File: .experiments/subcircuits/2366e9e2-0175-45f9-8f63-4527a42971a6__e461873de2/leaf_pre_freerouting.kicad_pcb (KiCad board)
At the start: 2 copper layers, 49.9 x 20.9 mm, 7 parts, among them J2 Output, J3 Debug, U5 AP2112K-3.3

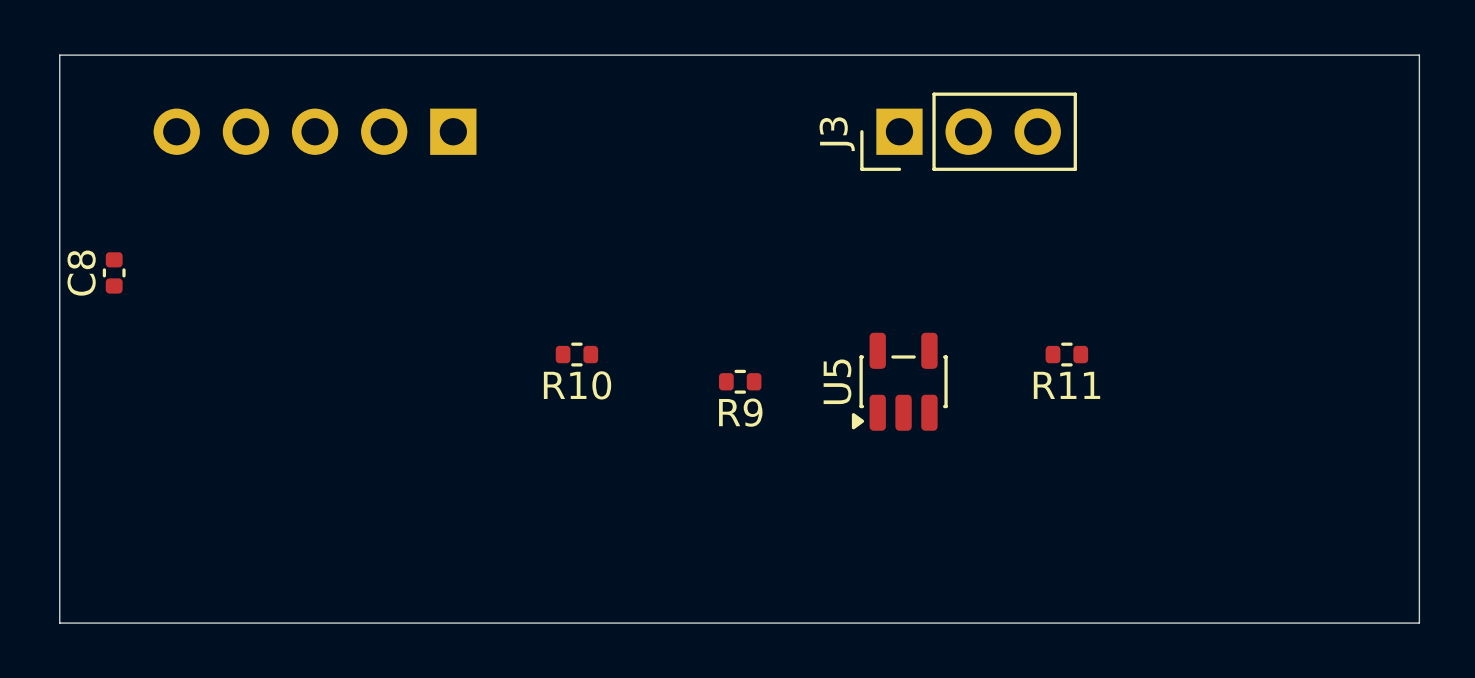
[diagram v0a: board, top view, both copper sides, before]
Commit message: feat: parent board stamping with preserved child copper
- Add --pcb, --stamp, --route, --jar flags to compose_subcircuits.py
- Implement subprocess-based parent board stamping (no pcbnew in main process)
- Add _stamp_parent_board() that copies base PCB, moves footprints to
  composed positions, clears existing tracks/zones, recreates child copper
  traces and vias with proper net name resolution
- Add _route_parent_board() for FreeRouting with preserve_existing_copper
- Add _persist_parent_artifact() for parent solved_layout.json persistence
- Store ParentComposition on ParentCompositionState for downstream access
- Update leaf artifacts from fresh pipeline run (6/6 leaves routed)
- Parent stamp verified: 37 components, 286 child traces, 10 vias preserved
  on real .kicad_pcb board with correct positions and net assignments
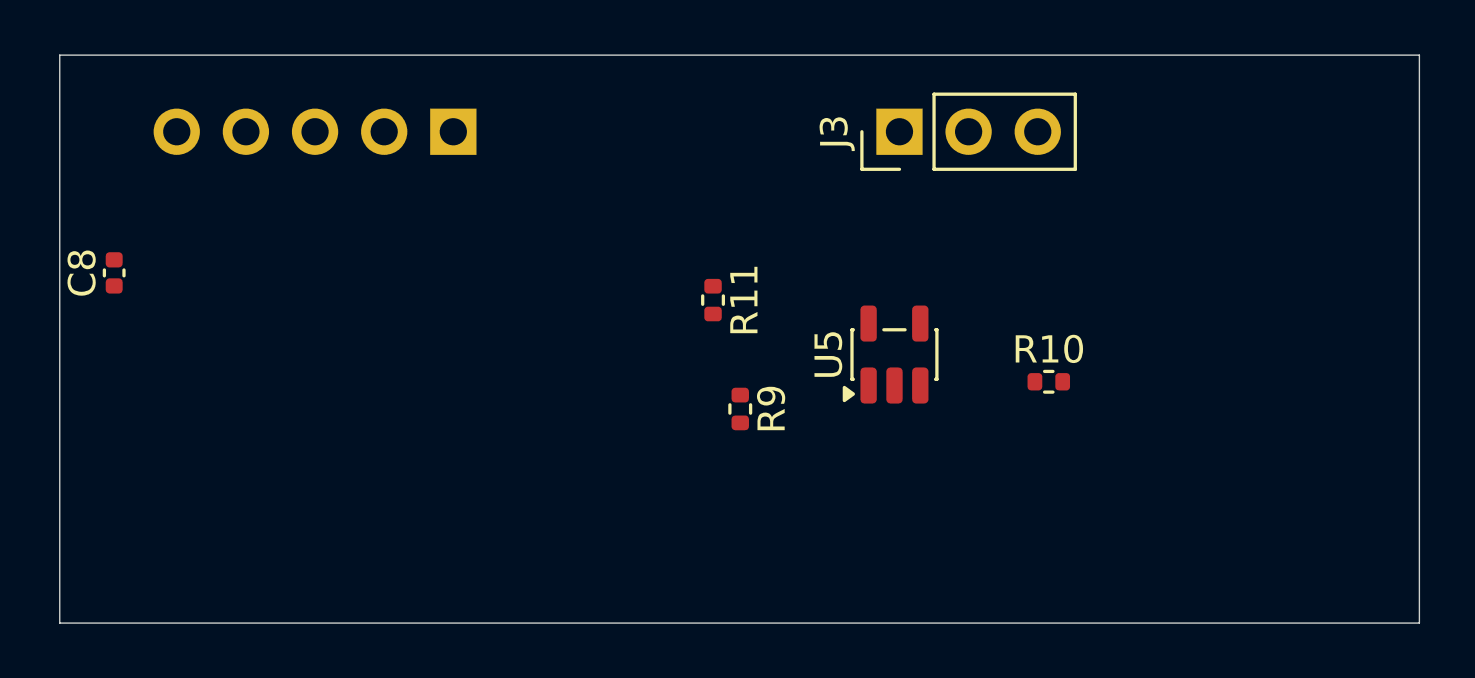
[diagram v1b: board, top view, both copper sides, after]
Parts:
- moved R10 17.4 mm to (36.3, 12.0), turned to 0 degrees
- moved R11 13.2 mm to (24.0, 9.00), turned to -90 degrees
- moved U5 1.05 mm to (30.7, 11.0)
- moved R9 1.00 mm to (25.0, 13.0), turned to -90 degrees
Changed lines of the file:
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@@
 	(footprint "Resistor_SMD:R_0402_1005Metric"
 		(layer "F.Cu")
-		(at 37 11 180)
+		(at 24 9 -90)
 		(descr "Resistor SMD 0402 (1005 Metric), square (rectangular) end terminal, IPC-7351 nominal, (Body size source: IPC-SM-782 page 72, https://www.pcb-3d.com/wordpress/wp-content/uploads/ipc-sm-782a_amendment_1_and_2.pdf), generated with kicad-footprint-generator")
 		(tags "resistor")
 		(property "Reference" "R11"
-			(at 0 -1.17 180)
+			(at 0 -1.17 270)
 			(layer "F.SilkS")
 			(effects
@@
 		)
 		(property "Value" "100k"
-			(at 0 1.17 180)
+			(at 0 1.17 270)
 			(layer "F.Fab")
 			(effects
@@
 		)
 		(property "Datasheet" ""
-			(at 0 0 180)
+			(at 0 0 270)
 			(layer "F.Fab")
 			(hide yes)
@@
 		)
 		(property "Description" ""
-			(at 0 0 180)
+			(at 0 0 270)
 			(layer "F.Fab")
 			(hide yes)
@@
 		)
 		(fp_text user "${REFERENCE}"
-			(at 0 0 180)
+			(at 0 0 270)
 			(layer "F.Fab")
 			(effects
@@
 		)
 		(pad "1" smd roundrect
-			(at -0.51 0 180)
+			(at -0.51 0 270)
 			(size 0.54 0.64)
 			(layers "F.Cu" "F.Mask" "F.Paste")
@@
 		)
 		(pad "2" smd roundrect
-			(at 0.51 0 180)
+			(at 0.51 0 270)
 			(size 0.54 0.64)
 			(layers "F.Cu" "F.Mask" "F.Paste")
@@
 	(footprint "Resistor_SMD:R_0402_1005Metric"
 		(layer "F.Cu")
-		(at 25 12 180)
+		(at 25 13 -90)
 		(descr "Resistor SMD 0402 (1005 Metric), square (rectangular) end terminal, IPC-7351 nominal, (Body size source: IPC-SM-782 page 72, https://www.pcb-3d.com/wordpress/wp-content/uploads/ipc-sm-782a_amendment_1_and_2.pdf), generated with kicad-footprint-generator")
 		(tags "resistor")
 		(property "Reference" "R9"
-			(at 0 -1.17 180)
+			(at 0 -1.17 270)
 			(layer "F.SilkS")
 			(effects
@@
 		)
 		(property "Value" "75k"
-			(at 0 1.17 180)
+			(at 0 1.17 270)
 			(layer "F.Fab")
 			(effects
@@
 		)
 		(property "Datasheet" ""
-			(at 0 0 180)
+			(at 0 0 270)
 			(layer "F.Fab")
 			(hide yes)
@@
 		)
 		(property "Description" ""
-			(at 0 0 180)
+			(at 0 0 270)
 			(layer "F.Fab")
 			(hide yes)
@@
 		)
 		(fp_text user "${REFERENCE}"
-			(at 0 0 180)
+			(at 0 0 270)
 			(layer "F.Fab")
 			(effects
@@
 		)
 		(pad "1" smd roundrect
-			(at -0.51 0 180)
+			(at -0.51 0 270)
 			(size 0.54 0.64)
 			(layers "F.Cu" "F.Mask" "F.Paste")
@@
 		)
 		(pad "2" smd roundrect
-			(at 0.51 0 180)
+			(at 0.51 0 270)
 			(size 0.54 0.64)
 			(layers "F.Cu" "F.Mask" "F.Paste")
@@
 	(footprint "Resistor_SMD:R_0402_1005Metric"
 		(layer "F.Cu")
-		(at 19 11 180)
+		(at 36.335 12)
 		(descr "Resistor SMD 0402 (1005 Metric), square (rectangular) end terminal, IPC-7351 nominal, (Body size source: IPC-SM-782 page 72, https://www.pcb-3d.com/wordpress/wp-content/uploads/ipc-sm-782a_amendment_1_and_2.pdf), generated with kicad-footprint-generator")
 		(tags "resistor")
 		(property "Reference" "R10"
-			(at 0 -1.17 180)
+			(at 0 -1.17 0)
 			(layer "F.SilkS")
 			(effects
@@
 		)
 		(property "Value" "10k"
-			(at 0 1.17 180)
+			(at 0 1.17 0)
 			(layer "F.Fab")
 			(effects
@@
 		)
 		(property "Datasheet" ""
-			(at 0 0 180)
+			(at 0 0 0)
 			(layer "F.Fab")
 			(hide yes)
@@
 		)
 		(property "Description" ""
-			(at 0 0 180)
+			(at 0 0 0)
 			(layer "F.Fab")
 			(hide yes)
@@
 		)
 		(attr smd)
+		(fp_line
+			(start -0.153641 -0.38)
+			(end 0.153641 -0.38)
+			(stroke
+				(width 0.12)
+				(type solid)
+			)
+			(layer "F.SilkS")
+		)
 		(fp_line
 			(start -0.153641 0.38)
@@
 			(layer "F.SilkS")
 		)
-		(fp_line
-			(start -0.153641 -0.38)
-			(end 0.153641 -0.38)
-			(stroke
-				(width 0.12)
-				(type solid)
-			)
-			(layer "F.SilkS")
-		)
 		(fp_rect
 			(start -0.93 -0.47)
@@
 		)
 		(fp_text user "${REFERENCE}"
-			(at 0 0 180)
+			(at 0 0 0)
 			(layer "F.Fab")
 			(effects
@@
 		)
 		(pad "1" smd roundrect
-			(at -0.51 0 180)
+			(at -0.51 0)
 			(size 0.54 0.64)
 			(layers "F.Cu" "F.Mask" "F.Paste")
@@
 		)
 		(pad "2" smd roundrect
-			(at 0.51 0 180)
+			(at 0.51 0)
 			(size 0.54 0.64)
 			(layers "F.Cu" "F.Mask" "F.Paste")
@@
 	(footprint "Package_TO_SOT_SMD:SOT-23-5"
 		(layer "F.Cu")
-		(at 31 12 90)
+		(at 30.665 11 90)
 		(descr "SOT, 5 Pin (JEDEC MO-178 Var AA https://www.jedec.org/document_search?search_api_views_fulltext=MO-178), generated with kicad-footprint-generator ipc_gullwing_generator.py")
 		(tags "SOT TO_SOT_SMD")

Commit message: feat: unified hierarchical solver (solve_hierarchy.py)
Single-command entry point for the full subcircuit pipeline:
  python3 solve_hierarchy.py LLUPS.kicad_sch --pcb LLUPS.kicad_pcb --route

Phase 1: Solve leaf subcircuits (delegates to solve_subcircuits.py)
  - 6 leaves solved and routed via FreeRouting
  - Canonical copper persisted in solved_layout.json

Phase 2: Compose and route parent (delegates to compose_subcircuits.py)
  - Grid layout of 6 children with 5mm spacing
  - Child copper preserved on stamped parent board
  - FreeRouting routes interconnect nets between subcircuits
  - Parent artifact persisted with full copper

Flags: --skip-leaves, --leaf-only, --rounds, --mode, --spacing-mm, --jar
Full pipeline completes in ~4 minutes (with routing)
Skip-leaves mode completes in ~28 seconds
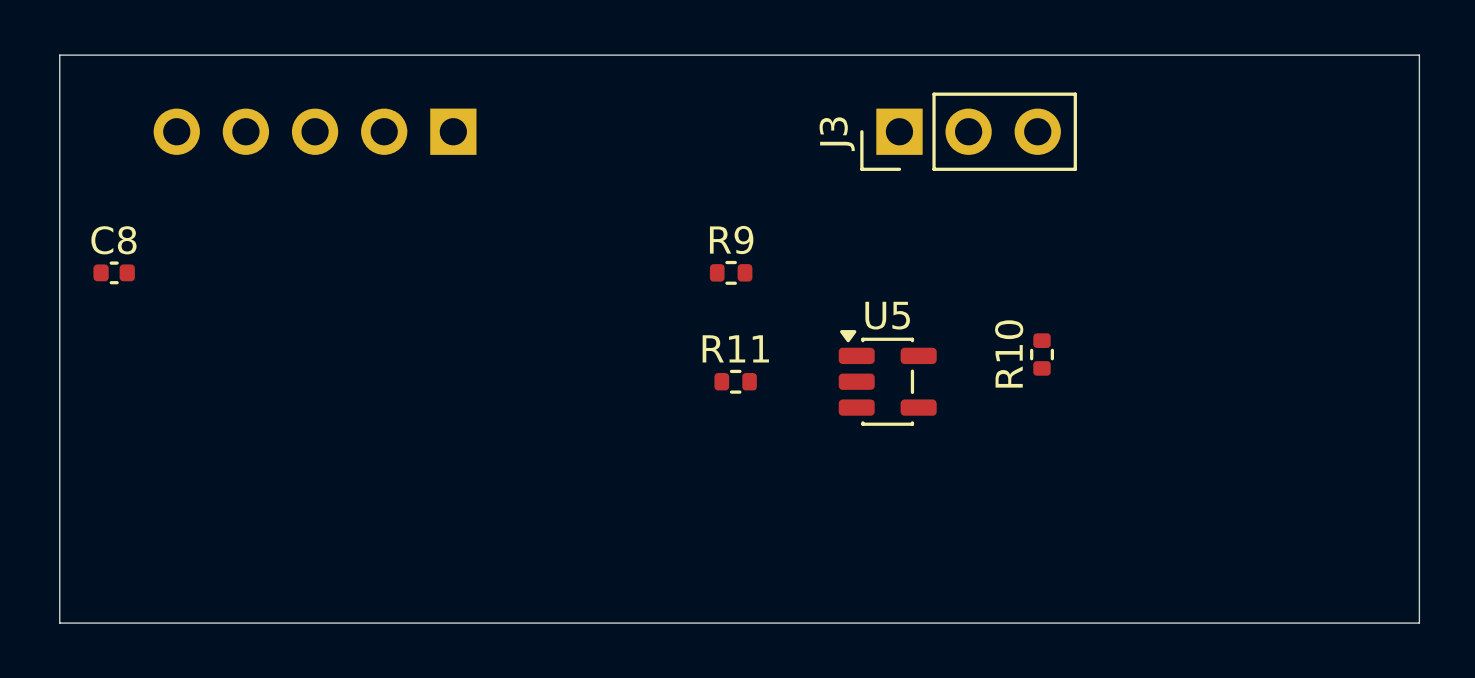
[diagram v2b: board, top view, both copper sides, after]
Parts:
- moved R9 5.01 mm to (24.7, 8.00), turned to 0 degrees
- moved R11 3.11 mm to (24.8, 12.0), turned to 0 degrees
- moved U5 1.03 mm to (30.4, 12.0), turned to 0 degrees
- moved R10 1.03 mm to (36.1, 11.0), turned to 90 degrees
- turned C8 to 0 degrees
